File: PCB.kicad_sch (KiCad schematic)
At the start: 56 parts, among them J1 USB_C_Receptacle_USB2.0_16P, J10 Conn_01x05_Pin, J11 Conn_01x05_Pin, J2 Conn_01x04_Pin, J3 Conn_01x04_Pin, J4 Conn_01x07_Pin, J5 Conn_01x02_Pin, J6 Conn_01x02_Pin, J7 Conn_01x02_Pin, J8 Conn_01x04_Pin, J9 Conn_01x07_Pin, SW1 SW_Push, SW2 SW_Push, U1 TMC2209_SILENTSTEPSTICK, U2 TMC2209_SILENTSTEPSTICK, U3 D3V3XA4B10LP, U4 AMS1117-3.3 (UMW), U5 TMC2209_SILENTSTEPSTICK, U6 ESP32-S3-WROOM-1

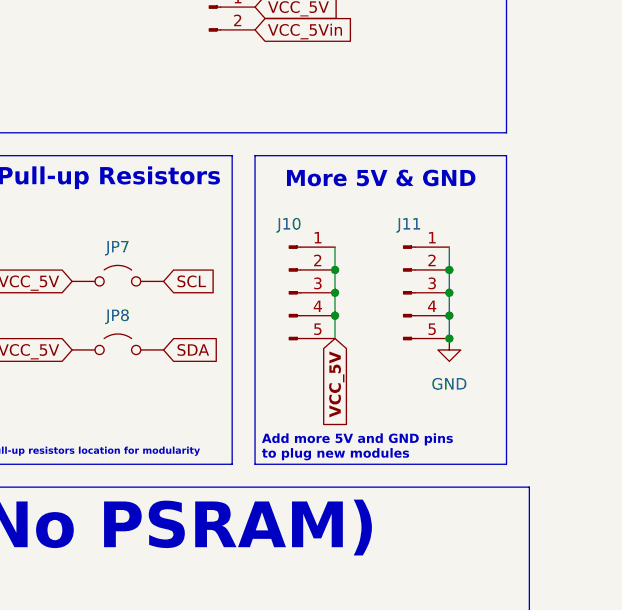
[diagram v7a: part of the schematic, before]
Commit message: ajout hub 3.3v
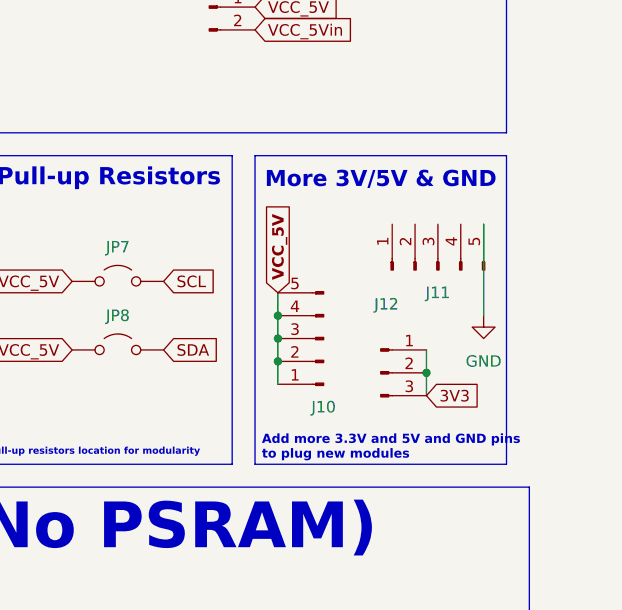
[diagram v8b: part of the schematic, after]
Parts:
- added J12: Conn_01x03_Pin, Connector_PinHeader_2.54mm:PinHeader_1x03_P2.54mm_Vertical, symbol Connector:Conn_01x03_Pin
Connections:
- net 3V3: now also J12.1 (Pin_1), J12.2 (Pin_2), J12.3 (Pin_3)
- net GND: no longer J11.1 (Pin_1), J11.2 (Pin_2), J11.3 (Pin_3), J11.4 (Pin_4)
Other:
- note added: "Add more 3.3V and 5V and GND pins to plug new modules"
- note added: "More 3V/5V & GND"
- note removed: "Add more 5V and GND pins to plug new modules"
- note removed: "More 5V & GND"
- moved on the sheet: J10, J11
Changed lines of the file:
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@@
 	)
 	(junction
-		(at 146.05 222.25)
+		(at 389.89 147.32)
 		(diameter 0)
 		(color 0 0 0 0)
 	)
 	(junction
-		(at 392.43 143.51)
+		(at 146.05 222.25)
 		(diameter 0)
 		(color 0 0 0 0)
@@
 	)
 	(junction
-		(at 379.73 135.89)
-		(diameter 0)
-		(color 0 0 0 0)
-	)
-	(junction
-		(at 392.43 138.43)
+		(at 373.38 146.05)
 		(diameter 0)
 		(color 0 0 0 0)
@@
 	)
 	(junction
-		(at 392.43 140.97)
-		(diameter 0)
-		(color 0 0 0 0)
-	)
-	(junction
-		(at 392.43 135.89)
-		(diameter 0)
-		(color 0 0 0 0)
-	)
-	(junction
-		(at 379.73 138.43)
+		(at 373.38 143.51)
 		(diameter 0)
 		(color 0 0 0 0)
@@
 	)
 	(junction
-		(at 379.73 140.97)
+		(at 373.38 140.97)
 		(diameter 0)
 		(color 0 0 0 0)
@@
 	(wire
 		(pts
+			(xy 389.89 144.78) (xy 389.89 147.32)
+		)
+		(stroke
+			(width 0)
+			(type default)
+		)
+	)
+	(wire
+		(pts
 			(xy 335.28 189.23) (xy 335.28 187.96)
 		)
@@
 	(wire
 		(pts
-			(xy 379.73 135.89) (xy 379.73 138.43)
+			(xy 373.38 146.05) (xy 373.38 143.51)
 		)
 		(stroke
@@
 	(wire
 		(pts
-			(xy 379.73 138.43) (xy 379.73 140.97)
+			(xy 373.38 143.51) (xy 373.38 140.97)
 		)
 		(stroke
@@
 	(wire
 		(pts
-			(xy 379.73 133.35) (xy 379.73 135.89)
-		)
-		(stroke
-			(width 0)
-			(type default)
-		)
-	)
-	(wire
-		(pts
-			(xy 392.43 138.43) (xy 392.43 140.97)
+			(xy 373.38 148.59) (xy 373.38 146.05)
 		)
 		(stroke
@@
 	(wire
 		(pts
-			(xy 379.73 140.97) (xy 379.73 143.51)
+			(xy 373.38 140.97) (xy 373.38 138.43)
 		)
 		(stroke
@@
 	(wire
 		(pts
-			(xy 392.43 140.97) (xy 392.43 143.51)
-		)
-		(stroke
-			(width 0)
-			(type default)
-		)
-	)
-	(wire
-		(pts
 			(xy 27.94 236.22) (xy 35.56 236.22)
 		)
@@
 	(wire
 		(pts
-			(xy 392.43 133.35) (xy 392.43 135.89)
+			(xy 396.24 130.81) (xy 396.24 140.97)
 		)
 		(stroke
@@
 	(wire
 		(pts
-			(xy 290.83 184.15) (xy 293.37 184.15)
+			(xy 389.89 147.32) (xy 389.89 149.86)
 		)
 		(stroke
@@
 	(wire
 		(pts
-			(xy 224.79 220.98) (xy 224.79 222.25)
+			(xy 290.83 184.15) (xy 293.37 184.15)
 		)
 		(stroke
@@
 	(wire
 		(pts
-			(xy 224.79 222.25) (xy 233.68 222.25)
+			(xy 224.79 220.98) (xy 224.79 222.25)
 		)
 		(stroke
@@
 	(wire
 		(pts
-			(xy 146.05 222.25) (xy 146.05 223.52)
+			(xy 224.79 222.25) (xy 233.68 222.25)
 		)
 		(stroke
@@
 	(wire
 		(pts
-			(xy 392.43 135.89) (xy 392.43 138.43)
+			(xy 146.05 222.25) (xy 146.05 223.52)
 		)
 		(stroke
@@
 		)
 	)
-	(text "Add more 5V and GND pins \nto plug new modules"
+	(text "Add more 3.3V and 5V and GND pins \nto plug new modules"
 		(exclude_from_sim no)
 		(at 371.602 155.702 0)
@@
 		)
 	)
-	(text "More 5V & GND"
+	(text "More 3V/5V & GND"
 		(exclude_from_sim no)
 		(at 384.81 125.984 0)
@@
 	(global_label "VCC_5V"
 		(shape input)
-		(at 379.73 143.51 270)
+		(at 373.38 138.43 90)
 		(fields_autoplaced yes)
 		(effects
@@
 				(bold yes)
 			)
-			(justify right)
+			(justify left)
 		)
 		(property "Intersheetrefs" "${INTERSHEET_REFS}"
-			(at 379.73 153.8655 90)
+			(at 373.38 128.0745 90)
 			(effects
 				(font
 					(size 1.27 1.27)
 				)
-				(justify right)
+				(justify left)
 				(hide yes)
 			)
@@
 		)
 	)
+	(global_label "3V3"
+		(shape input)
+		(at 389.89 149.86 0)
+		(fields_autoplaced yes)
+		(effects
+			(font
+				(size 1.27 1.27)
+			)
+			(justify left)
+		)
+		(property "Intersheetrefs" "${INTERSHEET_REFS}"
+			(at 396.3828 149.86 0)
+			(effects
+				(font
+					(size 1.27 1.27)
+				)
+				(justify left)
+				(hide yes)
+			)
+		)
+	)
 	(global_label "MOTORC1"
 		(shape input)
@@
 	(symbol
 		(lib_id "power:GND")
-		(at 392.43 143.51 0)
+		(at 396.24 140.97 0)
 		(unit 1)
 		(exclude_from_sim no)
@@
 		(fields_autoplaced yes)
 		(property "Reference" "#PWR033"
-			(at 392.43 149.86 0)
+			(at 396.24 147.32 0)
 			(effects
 				(font
@@
 		)
 		(property "Value" "GND"
-			(at 392.43 148.59 0)
+			(at 396.24 146.05 0)
 			(effects
 				(font
@@
 		)
 		(property "Footprint" ""
-			(at 392.43 143.51 0)
+			(at 396.24 140.97 0)
 			(effects
 				(font
@@
 		)
 		(property "Datasheet" ""
-			(at 392.43 143.51 0)
+			(at 396.24 140.97 0)
 			(effects
 				(font
@@
 		)
 		(property "Description" "Power symbol creates a global label with name \"GND\" , ground"
-			(at 392.43 143.51 0)
+			(at 396.24 140.97 0)
 			(effects
 				(font
@@
 	)
 	(symbol
+		(lib_id "Connector:Conn_01x03_Pin")
+		(at 384.81 147.32 0)
+		(unit 1)
+		(exclude_from_sim no)
+		(in_bom yes)
+		(on_board yes)
+		(dnp no)
+		(fields_autoplaced yes)
+		(property "Reference" "J12"
+			(at 385.445 139.7 0)
+			(effects
+				(font
+					(size 1.27 1.27)
+				)
+			)
+		)
+		(property "Value" "Conn_01x03_Pin"
+			(at 385.445 142.24 0)
+			(effects
+				(font
+					(size 1.27 1.27)
+				)
+				(hide yes)
+			)
+		)
+		(property "Footprint" "Connector_PinHeader_2.54mm:PinHeader_1x03_P2.54mm_Vertical"
+			(at 384.81 147.32 0)
+			(effects
+				(font
+					(size 1.27 1.27)
+				)
+				(hide yes)
+			)
+		)
+		(property "Datasheet" "~"
+			(at 384.81 147.32 0)
+			(effects
+				(font
+					(size 1.27 1.27)
+				)
+				(hide yes)
+			)
+		)
+		(property "Description" "Generic connector, single row, 01x03, script generated"
+			(at 384.81 147.32 0)
+			(effects
+				(font
+					(size 1.27 1.27)
+				)
+				(hide yes)
+			)
+		)
+		(pin "2"
+		)
+		(pin "3"
+		)
+		(pin "1"
+		)
+		(instances
+			(project ""
+				(path "/ea97f20c-9bc4-49f4-bc03-d8d68656df8b"
+					(reference "J12")
+					(unit 1)
+				)
+			)
+		)
+	)
+	(symbol
 		(lib_id "Connector:Conn_01x05_Pin")
-		(at 387.35 138.43 0)
+		(at 391.16 135.89 90)
 		(unit 1)
 		(exclude_from_sim no)
@@
 		(fields_autoplaced yes)
 		(property "Reference" "J11"
-			(at 387.985 130.81 0)
+			(at 391.16 138.43 90)
 			(effects
 				(font
@@
 		)
 		(property "Value" "Conn_01x05_Pin"
-			(at 387.985 130.81 0)
+			(at 383.54 135.255 0)
 			(effects
 				(font
@@
 		)
 		(property "Footprint" "Connector_PinHeader_2.54mm:PinHeader_1x05_P2.54mm_Vertical"
-			(at 387.35 138.43 0)
+			(at 391.16 135.89 0)
 			(effects
 				(font
@@
 		)
 		(property "Datasheet" "~"
-			(at 387.35 138.43 0)
+			(at 391.16 135.89 0)
 			(effects
 				(font
@@
 		)
 		(property "Description" "Generic connector, single row, 01x05, script generated"
-			(at 387.35 138.43 0)
+			(at 391.16 135.89 0)
 			(effects
 				(font
@@
 	(symbol
 		(lib_id "Connector:Conn_01x05_Pin")
-		(at 374.65 138.43 0)
+		(at 378.46 143.51 180)
 		(unit 1)
 		(exclude_from_sim no)
@@
 		(dnp no)
 		(property "Reference" "J10"
-			(at 374.65 130.81 0)
+			(at 378.46 151.13 0)
 			(effects
 				(font
@@
 		)
 		(property "Value" "Conn_01x05_Pin"
-			(at 375.285 130.81 0)
+			(at 377.825 151.13 0)
 			(effects
 				(font
@@
 		)
 		(property "Footprint" "Connector_PinHeader_2.54mm:PinHeader_1x05_P2.54mm_Vertical"
-			(at 374.65 138.43 0)
+			(at 378.46 143.51 0)
 			(effects
 				(font
@@
 		)
 		(property "Datasheet" "~"
-			(at 374.65 138.43 0)
+			(at 378.46 143.51 0)
 			(effects
 				(font
@@
 		)
 		(property "Description" "Generic connector, single row, 01x05, script generated"
-			(at 374.65 138.43 0)
+			(at 378.46 143.51 0)
 			(effects
 				(font
